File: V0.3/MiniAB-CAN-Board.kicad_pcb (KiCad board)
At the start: 2 copper layers, 51 x 45 mm, 121 parts, among them J1 PC-FAN, J10 USB_B_Micro, J11 ENDSTOP1, J12 CAN, J13 ENDSTOP2, J14 PROBE, J2 PC-FAN, J3 HE-FAN, J4 TH0, J5 H0, J6 STEPPER, J7 NEOPIXEL, J8 I2C, J9 Conn_02x03_Top_Bottom, Q1 AO3400A, Q2 AO3400A, Q3 AON7418, U1 ADXL345BCCZ-RL7, U2 STM32F103C8Tx, U3 74LVC1G17, U4 LP5907MFX-3.3, U5 TMC2209-LA, U6 TPS54202DDC, U7 TCAN330, Y1 8MHz

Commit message: PCB Layout V0.3 WIP
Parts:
- removed R27: 510k, Resistor_SMD:R_0603_1608Metric
- removed R28: 100k, Resistor_SMD:R_0603_1608Metric
- J10: footprint Connector_USB:USB_Micro-B_Molex-105017-0001 -> Connector_USB:USB_Micro-B_Molex-105133-0001
- J5: moved to B.Cu
- moved J5 216.5 mm to (194.3, 29.8), turned to -90 degrees
- moved C43 216.2 mm to (218.5, 26.2)
- moved U6 197.8 mm to (217.5, 29.1), turned to 90 degrees
- moved C34 191.8 mm to (215.0, 28.5), turned to -90 degrees
- moved U4 189.4 mm to (215.9, 53.1)
- moved D4 184.9 mm to (221.3, 22.4), turned to -90 degrees
- moved C17 183.2 mm to (218.8, 52.9), turned to -90 degrees
- moved R15 180.9 mm to (221.3, 19.1), turned to 90 degrees
- moved C42 180.3 mm to (212.7, 32.6)
- moved R37 179.3 mm to (207.0, 36.4), turned to 180 degrees
- moved C22 177.0 mm to (217.6, 32.8), turned to 180 degrees
- moved C21 176.2 mm to (217.6, 34.6), turned to 180 degrees
- moved R19 163.0 mm to (220.3, 52.9), turned to -90 degrees
- moved C38 160.1 mm to (212.7, 34.6)
- moved D6 159.6 mm to (219.8, 50.3), turned to 180 degrees
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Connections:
- net Net-(C34-Pad2) renamed /SW
- net Net-(C43-Pad2) renamed /FB
- J12 pad 1: TMC_VS -> GND
- J12 pad 2: GND -> TMC_VS
- J5 pad 1: Net-(D3-Pad1) -> TMC_VS
- J5 pad 2: TMC_VS -> Net-(D3-Pad1)
- Q3 pad 2: Net-(Q3-Pad2) -> GND
- Q3 pad 3: Net-(D3-Pad1) -> GND
- Q3 pad 4: (no net) -> Net-(Q3-Pad2)
- Q3 pad 5: (no net) -> Net-(D3-Pad1)
- Q3 pad 6: (no net) -> Net-(D3-Pad1)
- Q3 pad 7: (no net) -> Net-(D3-Pad1)
- Q3 pad 8: (no net) -> Net-(D3-Pad1)
- U6 pad 5: Net-(R27-Pad2) -> unconnected-(U6-Pad5)
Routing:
- net /FB: track 0.00 -> 21.9 mm, vias 0 -> 2
- net Net-(C43-Pad1): track 0.00 -> 16.0 mm, vias 0 -> 2
- net +5V: track 0.00 -> 10.6 mm
- net /SW: track 0.00 -> 7.40 mm, vias 0 -> 4
- net GND: track 25.1 -> 31.9 mm, vias 22 -> 31
- net CAN_TX: track 1.93 -> 6.32 mm
- net VBAT: track 0.00 -> 3.50 mm
- net CAN_RX: track 1.93 -> 4.92 mm
- net Net-(D6-Pad1): track 0.00 -> 1.87 mm
- net Net-(C34-Pad1): track 0.00 -> 1.62 mm
- net Net-(D5-Pad1): track 0.00 -> 1.56 mm
- added copper zone on F.Cu, net +5V
- added copper zone on B.Cu, net /SW
- added copper zone on F.Cu, net /SW
- added copper zone on F.Cu, net GND
- added copper zone on F.Cu, net Net-(D3-Pad1)
- added copper zone on F.Cu, net TMC_VS
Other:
- copper layers 2 -> 4

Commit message: Updated footprints to 0402 if possible
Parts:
- C10, C11, C12, C13, C14, C15, C16, C17, C18, C2, C20, C22, C23, C24, C26, C27, C28, C29, C3, C30, C33, C34, C35, C4, C40, C41, C43, C5, C6, C7, C8, C9: footprint Capacitor_SMD:C_0603_1608Metric -> Capacitor_SMD:C_0402_1005Metric
- D1, D2, D3, D4, D5, D6, D7: footprint LED_SMD:LED_0805_2012Metric -> LED_SMD:LED_0402_1005Metric
- D9: footprint LED_SMD:LED_0603_1608Metric -> LED_SMD:LED_0402_1005Metric
- FB1: value FerriteBead_Small -> GZ1608D601TF
- R1, R10, R11, R12, R13, R14, R15, R16, R17, R18, R19, R2, R20, R21, R22, R23, R24, R25, R26, R29, R34, R35, R36, R4, R6, R7, R8, R9: footprint Resistor_SMD:R_0603_1608Metric -> Resistor_SMD:R_0402_1005Metric
- moved R14 204.6 mm to (236.2, 48.8), turned to 180 degrees
- moved FB2 204.4 mm to (236.1, 53.1)
- moved C1 200.0 mm to (240.6, 48.2), turned to 180 degrees
- moved R13 197.4 mm to (237.0, 50.3), turned to 90 degrees
- moved C4 194.3 mm to (238.8, 46.7)
- moved C12 191.7 mm to (235.6, 50.8)
- moved C14 187.9 mm to (235.6, 49.8)
- moved FB1 186.6 mm to (239.0, 50.1)
- moved C13 181.5 mm to (235.6, 51.8)
- moved C3 177.2 mm to (242.0, 46.7), turned to 180 degrees
- moved C6 175.4 mm to (227.8, 40.4), turned to 90 degrees
- moved C10 171.0 mm to (225.8, 48.4), turned to -90 degrees
- moved C8 168.2 mm to (236.2, 41.5)
- moved C11 159.2 mm to (224.8, 48.4), turned to -90 degrees
- moved C9 156.8 mm to (227.7, 49.9), turned to -90 degrees
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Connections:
- J12 pad 1: GND -> CANL
- J12 pad 2: TMC_VS -> CANH
- J12 pad 3: CANL -> GND
- J12 pad 4: CANH -> TMC_VS
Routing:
- net VBAT: track 3.50 -> 26.6 mm, vias 0 -> 10
- net ADXL_INT1: track 0.00 -> 10.0 mm, vias 0 -> 2
- net ADXL_CS: track 0.00 -> 8.90 mm, vias 0 -> 2
- net Net-(C43-Pad1): track 16.0 -> 24.1 mm
- net +5V: track 10.6 -> 2.87 mm
- net SDO: track 0.00 -> 6.51 mm
- net Net-(C1-Pad1): track 0.00 -> 5.90 mm
- net VDDA: track 0.00 -> 5.79 mm
- net SCLK: track 0.00 -> 5.29 mm
- net SDI: track 0.00 -> 5.10 mm
- net TMC_VS: track 0.00 -> 4.62 mm
- net CAN_RX: track 4.92 -> 8.08 mm
- net GND: track 31.9 -> 28.8 mm, vias 31 -> 42
- net TH0: track 0.00 -> 2.34 mm
- net CAN_TX: track 6.32 -> 8.64 mm
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- added copper zone on In2.Cu, net GND
- added copper zone on F.Cu, net VBAT
- added copper zone on In1.Cu, net VBAT

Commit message: Finished Front Side
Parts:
- removed the C19 at (181.4, 24.5)
- added C15: 1u, Capacitor_SMD:C_0402_1005Metric, F.Cu at (217.8, 52.2)
- added C45: 10u/35V, Capacitor_SMD:C_0805_2012Metric, F.Cu at (217.7, 36.9)
- added C46: 22u, Capacitor_SMD:C_0805_2012Metric, F.Cu at (215.0, 38.5)
- added R32: 100k, Resistor_SMD:R_0402_1005Metric, F.Cu at (239.2, 39.9)
- J9, JP2: moved to B.Cu
- JP1: value HEF -> PCF; moved to B.Cu
- moved J11 241.4 mm to (229.7, 99.5)
- moved J4 241.4 mm to (240.1, 86.8)
- moved J8 241.4 mm to (204.3, 86.8)
- moved J13 241.4 mm to (217.0, 99.0)
- moved J14 241.4 mm to (217.0, 86.8)
- moved J3 241.4 mm to (250.5, 86.8)
- moved J7 241.4 mm to (228.6, 86.8)
- moved C37 229.6 mm to (236.1, 29.5), turned to -135 degrees
- moved D9 226.7 mm to (225.8, 44.5), turned to 90 degrees
- moved C38 221.4 mm to (240.9, 37.0), turned to 45 degrees
- moved U3 214.2 mm to (221.1, 47.0), turned to 180 degrees
- moved J6 208.5 mm to (237.8, 24.3), turned to -45 degrees
- moved R28 207.8 mm to (239.3, 33.8), turned to 135 degrees
- moved C21 194.0 mm to (224.8, 57.5), turned to 180 degrees
- moved C42 193.4 mm to (233.9, 39.0), turned to 45 degrees
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- renumbered C15 to C16, C16 to C17, C17 to C18, C18 to C19, C20 to C21, C21 to C22, C22 to C27, C27 to C28, C28 to C29, C29 to C30, C30 to C31, C31 to C32, C32 to C33, C33 to C34, C34 to C35, C35 to C36, C36 to C37, C37 to C38, C38 to C39, C39 to C40, C40 to C41, C41 to C42, C42 to C43, C43 to C44, R12 to R10, R13 to R11, R14 to R12, R15 to R13, R16 to R14, R17 to R15, R18 to R16, R19 to R17, R20 to R18, R21 to R19, R22 to R20, R23 to R21, R24 to R22, R25 to R23, R26 to R24, R29 to R25, R30 to R26, R31 to R27, R32 to R28, R33 to R29, R4 to R3, R34 to R30, R35 to R31, R36 to R33, R37 to R34, R38 to R35, R6 to R4, R7 to R5, R8 to R6, R9 to R7, R10 to R8, R11 to R9
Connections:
- J6 pad 1: A1 -> B2
- J6 pad 2: A2 -> B1
- J6 pad 3: B1 -> A1
- J6 pad 4: B2 -> A2
- Q3 pad 2: GND -> Net-(Q3-Pad2)
- Q3 pad 3: GND -> Net-(D3-Pad1)
- R23 pad 1: +5V -> VBAT
- U2 pad 18: unconnected-(U2-Pad18) -> NEOPIXEL
- U2 pad 19: unconnected-(U2-Pad19) -> ST_ENN
- U5 pad 20: GND -> Net-(R32-Pad1)
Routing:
- net Net-(J1-Pad2): track 0.00 -> 89.0 mm, vias 0 -> 1
- net Net-(D1-Pad1): track 0.00 -> 55.3 mm, vias 0 -> 1
- net TMC_VS: track 4.62 -> 56.3 mm, vias 0 -> 7
- net ST_ENN: track 0.00 -> 42.2 mm, vias 0 -> 2
- net +5V: track 2.87 -> 40.3 mm, vias 0 -> 3
- net Net-(J3-Pad2): track 0.00 -> 25.4 mm, vias 0 -> 1
- net ST_DIR: track 0.00 -> 14.5 mm, vias 0 -> 2
- net GND: track 28.8 -> 40.5 mm, vias 42 -> 264
- net VBAT: track 26.6 -> 37.9 mm, vias 10 -> 16
- net ST_DIAG: track 0.00 -> 9.47 mm
- net Net-(R32-Pad1): track 0.00 -> 6.55 mm
- net ST_RX: track 0.00 -> 5.80 mm
- net ST_STEP: track 0.00 -> 4.26 mm, vias 0 -> 2
- net ST_TX: track 0.00 -> 2.76 mm
- net Net-(D3-Pad1): track 0.00 -> 2.75 mm
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- added copper zone on B.Cu, net A1
- added copper zone on F.Cu, net A1
- added copper zone on B.Cu, net A2
- added copper zone on F.Cu, net A2
- added copper zone on B.Cu, net B1
- added copper zone on F.Cu, net B1
- added copper zone on B.Cu, net B2
- added copper zone on F.Cu, net B2
- added copper zone on F.Cu, net BRA
- added copper zone on F.Cu, net BRB
- added copper zone on B.Cu, net GND

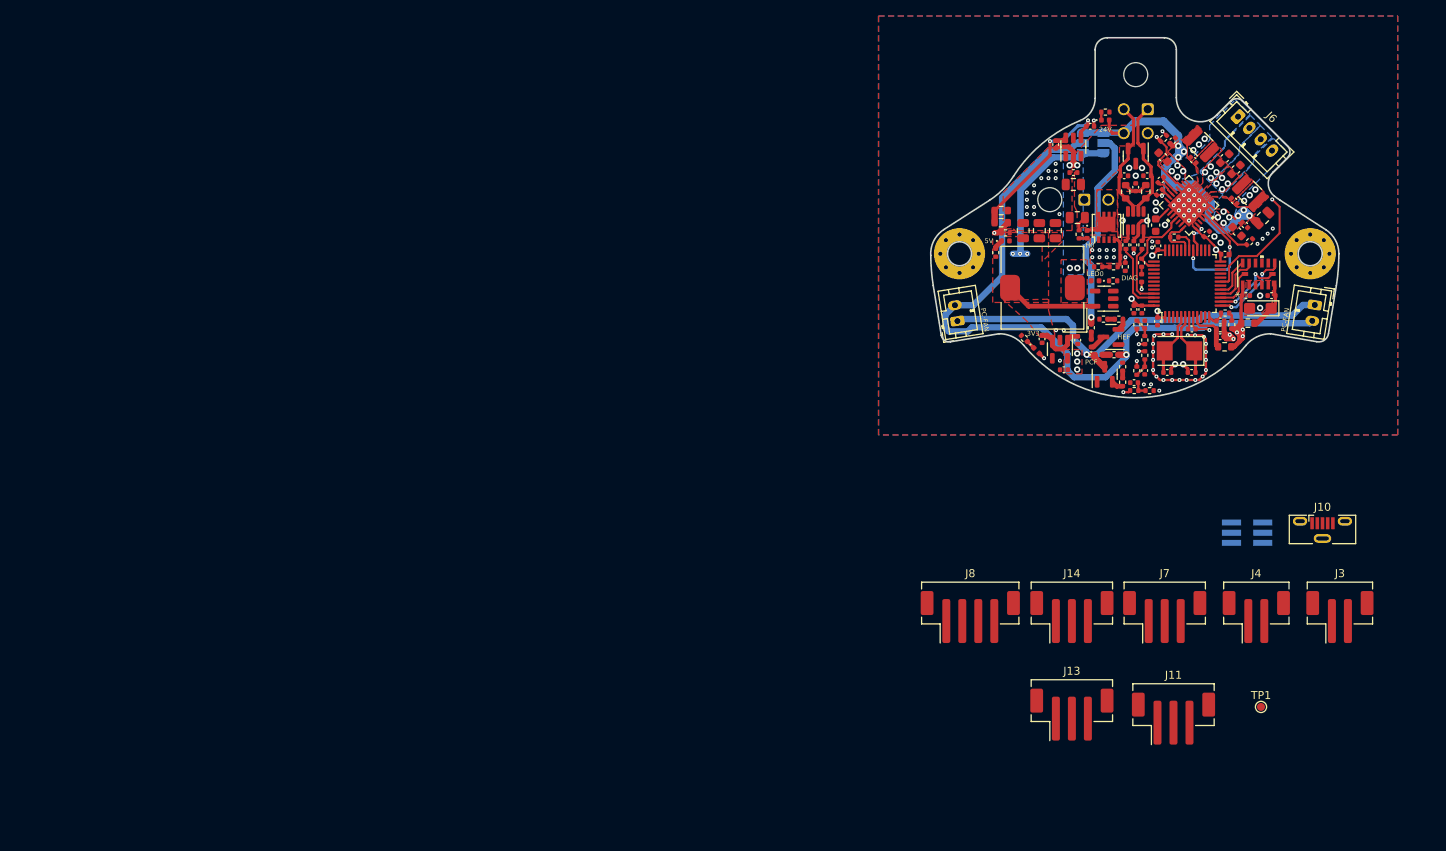
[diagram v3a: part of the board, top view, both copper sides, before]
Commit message: Update Fan Mosfet Placement
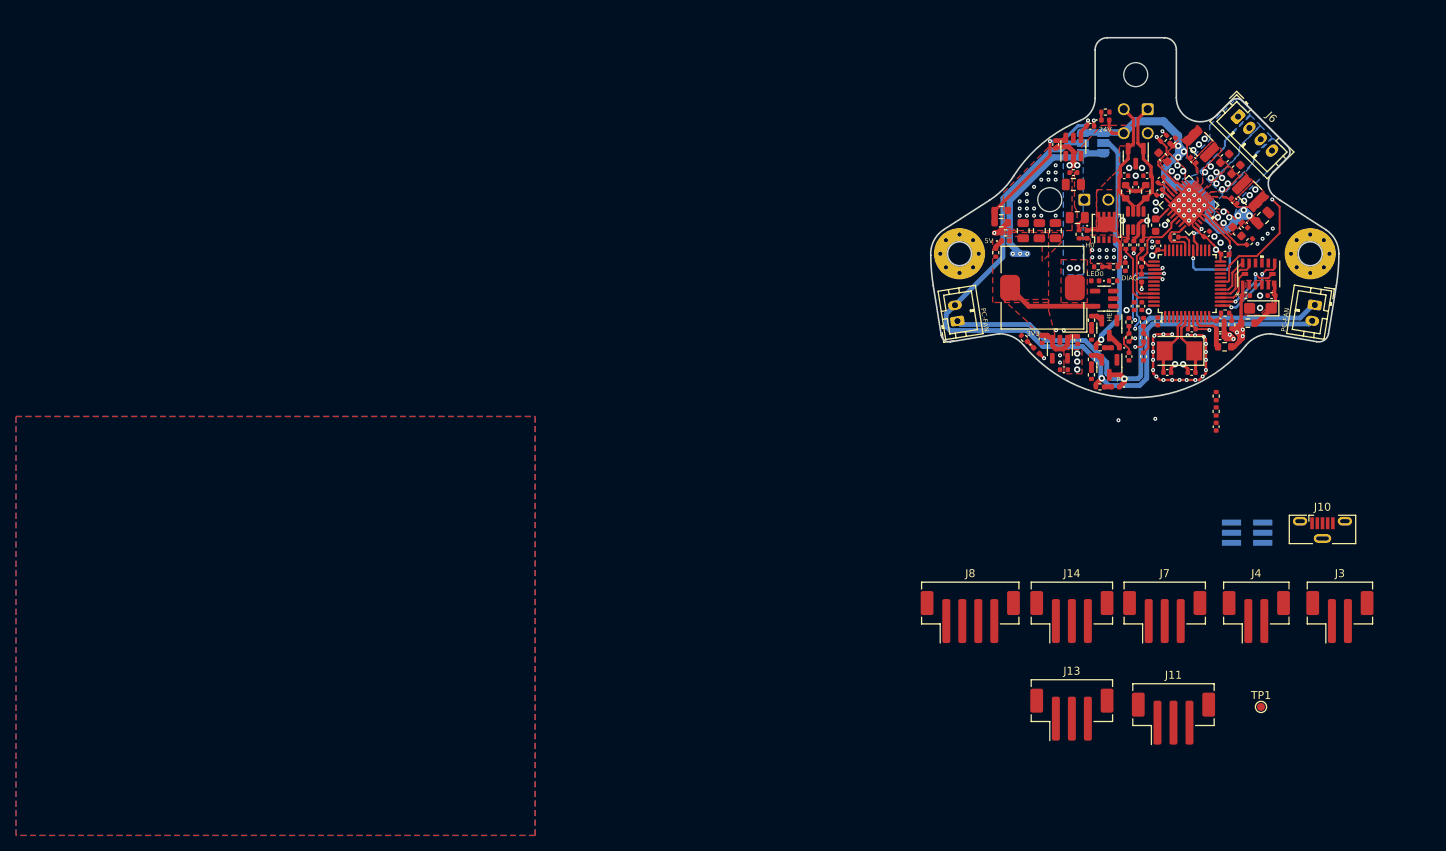
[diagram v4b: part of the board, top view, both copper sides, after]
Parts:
- moved C21 11.6 mm to (235.1, 63.0), turned to -90 degrees
- moved R21 10.3 mm to (235.1, 59.2), turned to 90 degrees
- moved R22 8.72 mm to (235.1, 61.1), turned to 90 degrees
- moved R2 4.82 mm to (219.5, 54.6), turned to -90 degrees
- moved R18 4.60 mm to (224.2, 50.0)
- moved D1 4.54 mm to (222.5, 58.1), turned to 180 degrees
- moved R3 4.39 mm to (220.6, 58.1), turned to 0 degrees
- moved R19 4.26 mm to (224.2, 51.9), turned to 90 degrees
- moved R1 4.04 mm to (219.5, 56.6), turned to 90 degrees
- moved C17 4.01 mm to (226.0, 54.3), turned to -90 degrees
- moved R6 3.42 mm to (219.5, 49.7), turned to -90 degrees
- moved D2 3.08 mm to (222.5, 53.2), turned to 180 degrees
- moved R7 2.73 mm to (220.6, 53.2), turned to 0 degrees
- moved C19 2.63 mm to (224.2, 54.3)
- moved R5 2.54 mm to (219.5, 51.7), turned to 90 degrees
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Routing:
- net GND: track 40.5 -> 19.3 mm, vias 264 -> 245
- net ENDSTOP2: track 2.33 -> 14.9 mm, vias 0 -> 2
- net ENDSTOP1: track 2.35 -> 14.6 mm, vias 0 -> 2
- net VBAT: track 37.9 -> 49.8 mm, vias 16 -> 35
- net Net-(D1-Pad1): track 55.3 -> 59.2 mm
- net Net-(J3-Pad2): track 25.4 -> 28.3 mm
- net +5V: track 40.3 -> 41.4 mm
- net Net-(D1-Pad2): track 1.87 -> 0.94 mm
- net Net-(J1-Pad2): track 89.0 -> 89.9 mm
- net Net-(J11-Pad3): track 0.70 -> 1.57 mm
- net PROBE: track 1.91 -> 1.17 mm, vias 0 -> 1

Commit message: Stuck on connector placement
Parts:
- J11, J14: moved to B.Cu
- moved J10 68.3 mm to (207.1, 21.5)
- moved J14 57.7 mm to (256.4, 44.6), turned to -90 degrees
- moved J11 57.5 mm to (213.1, 44.5), turned to -90 degrees
- moved J9 31.2 mm to (231.7, 46.0), turned to 90 degrees
- moved C21 23.9 mm to (241.3, 40.0), turned to -45 degrees
- moved R22 23.0 mm to (242.0, 39.2), turned to 135 degrees
- moved R21 22.0 mm to (242.7, 38.5), turned to -45 degrees
- moved R25 0.56 mm to (230.2, 38.9), turned to 135 degrees
- moved J4 0.45 mm to (240.4, 86.6)
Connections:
- C7 pad 2: Net-(C7-Pad2) -> NRST
- U2 pad 7: Net-(C7-Pad2) -> NRST
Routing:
- net PROBE: track 1.17 -> 36.3 mm, vias 1 -> 2
- net Net-(J11-Pad3): track 1.57 -> 16.0 mm
- net SWCLK: track 0.00 -> 9.79 mm, vias 0 -> 1
- net Net-(R4-Pad2): track 0.68 -> 7.95 mm, vias 1 -> 2
- net BOOT1: track 0.00 -> 6.74 mm, vias 0 -> 1
- net SWDIO: track 0.00 -> 4.56 mm, vias 0 -> 1
- net NRST: track 0.00 -> 3.97 mm, vias 0 -> 1
- net ST_DIR: track 14.5 -> 11.3 mm
- net Net-(J1-Pad2): track 89.9 -> 92.8 mm
- net LED0: track 0.00 -> 2.22 mm, vias 0 -> 1
- net ST_ENN: track 42.2 -> 43.8 mm
- net Net-(C7-Pad2): track 1.57 -> 0.00 mm
- net SDA: track 0.00 -> 1.22 mm, vias 0 -> 1
- net PC-FAN: track 0.91 -> 2.12 mm, vias 0 -> 1
- net HEATER: track 0.90 -> 2.11 mm, vias 0 -> 1
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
